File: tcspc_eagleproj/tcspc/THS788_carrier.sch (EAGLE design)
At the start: 46 parts, among them J1 BXE-040-01-F-D-A_BSE, U1 THS788

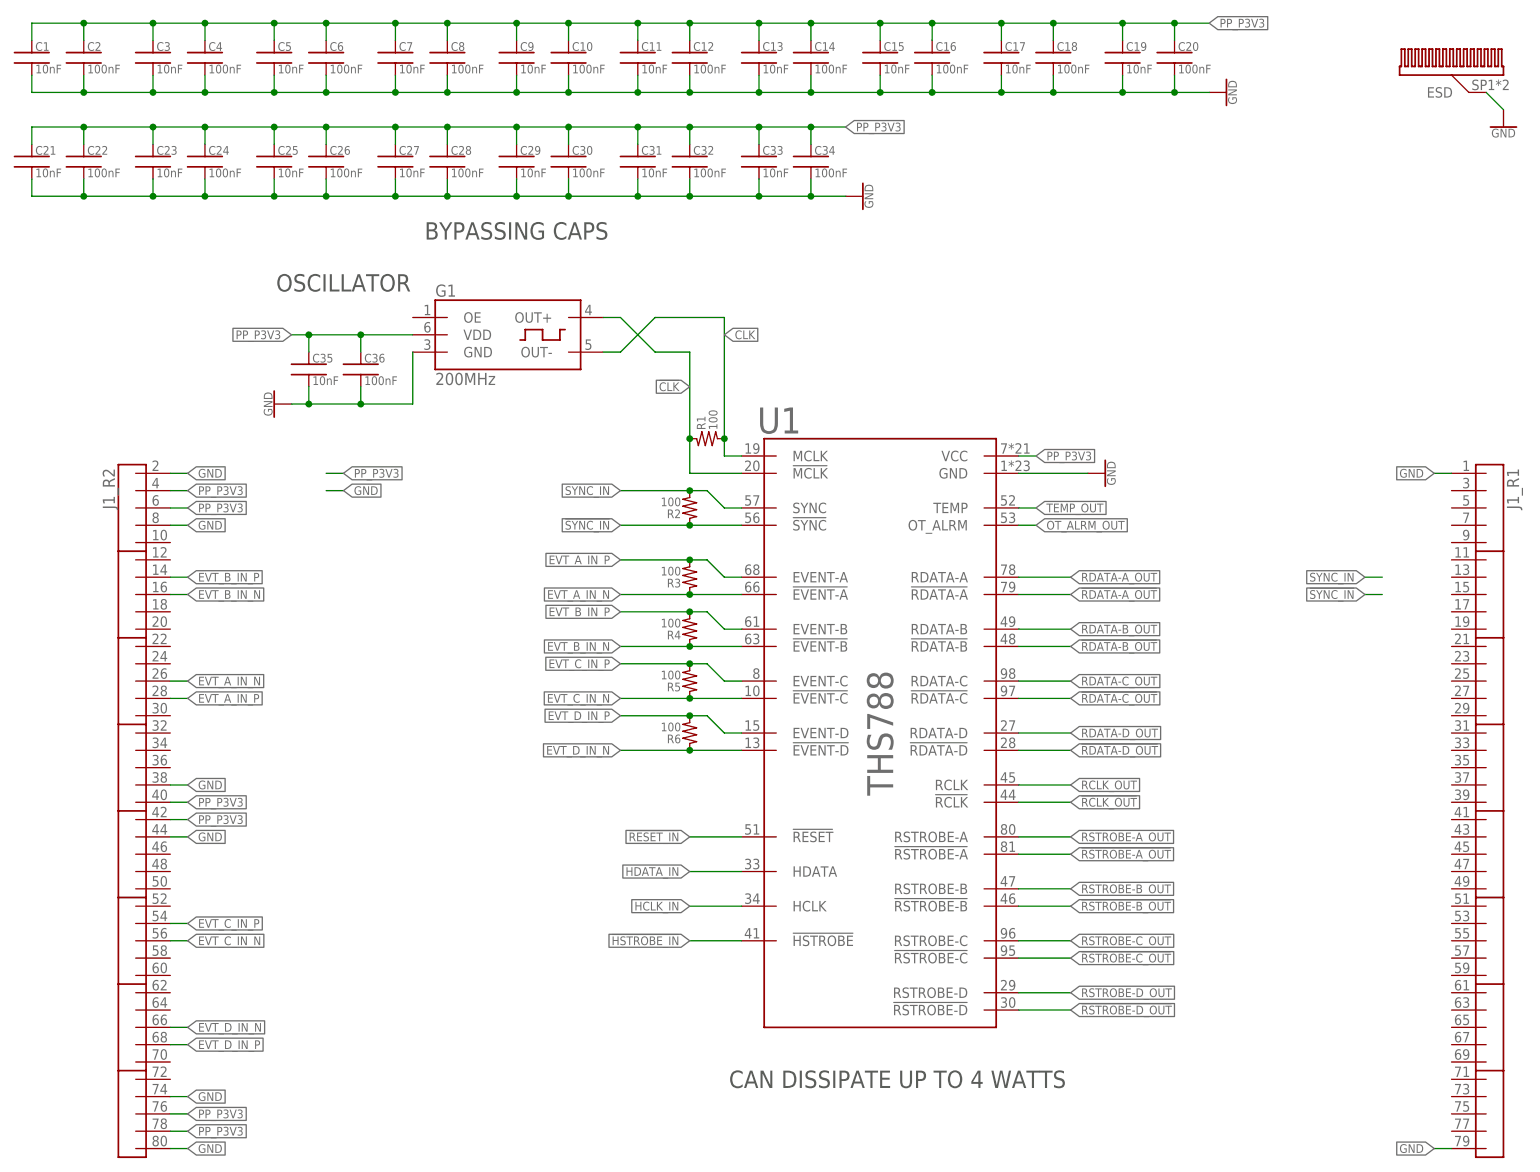
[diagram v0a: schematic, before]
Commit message: Did a little more work on the THS788 carrier, routed a few more HS diff signals
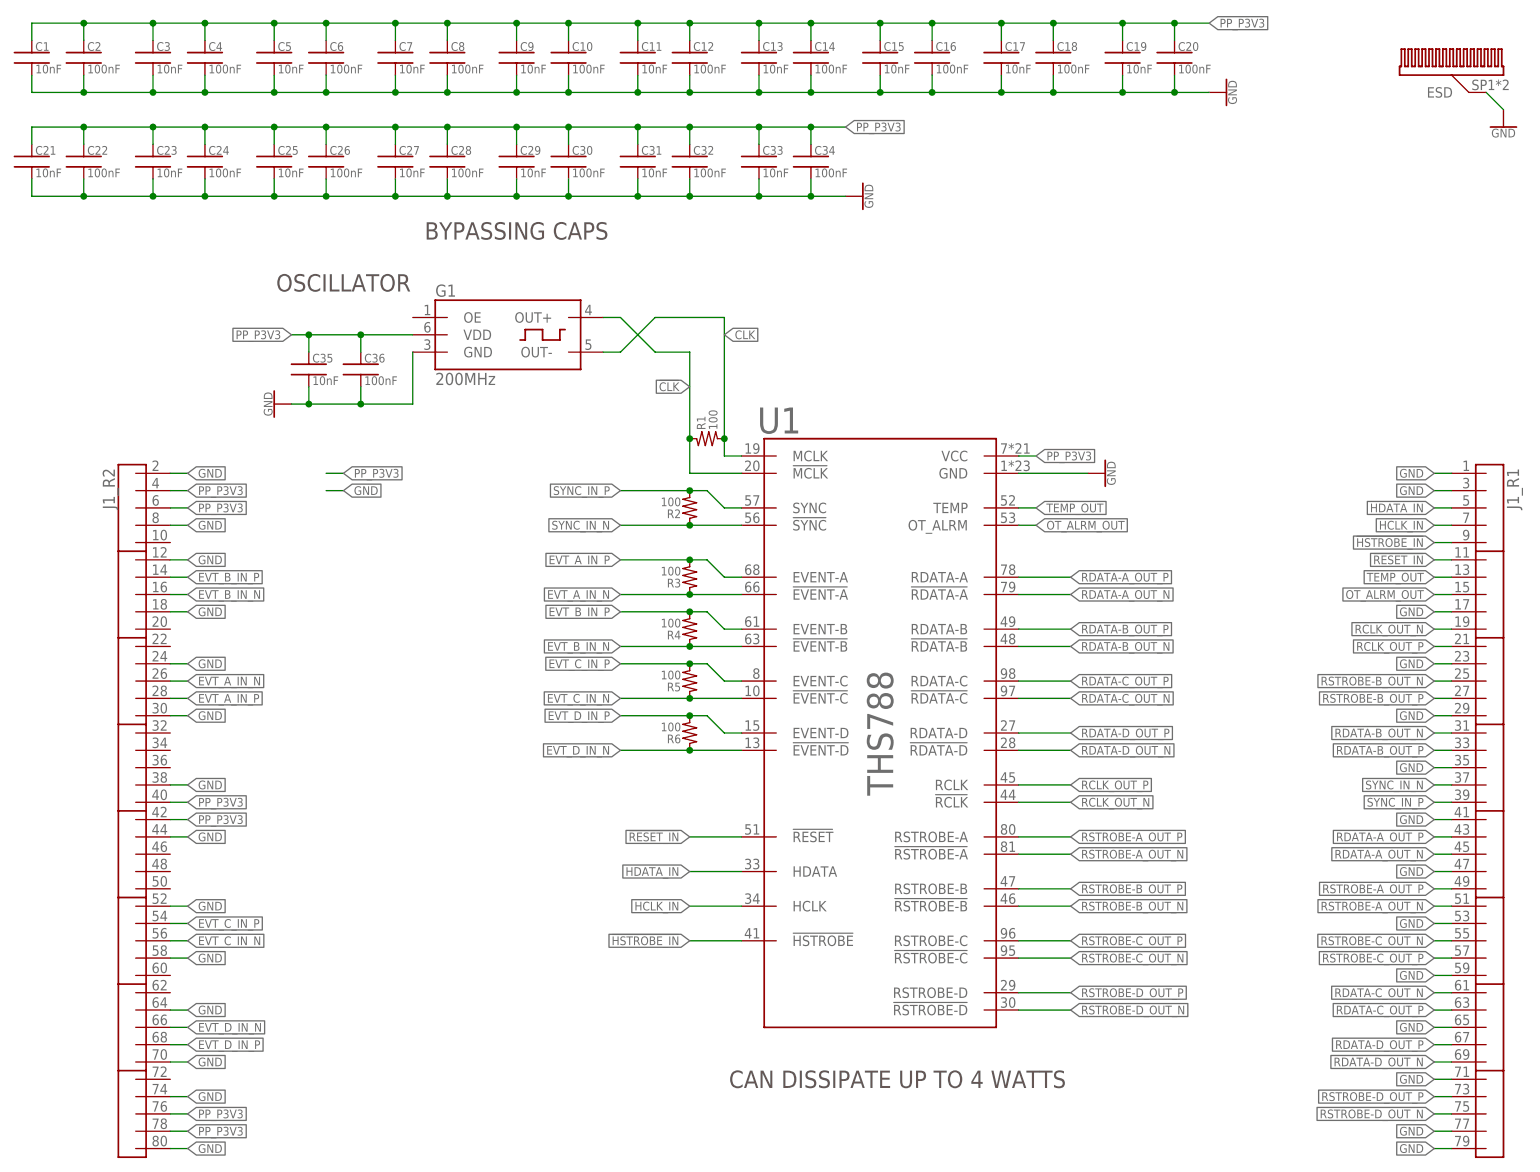
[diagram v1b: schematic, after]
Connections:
- removed net !RCLK_OUT: U1.!RCLK
- removed net !RDATA-A_OUT: U1.!RDATA-A
- removed net !RDATA-B_OUT: U1.!RDATA-B
- removed net !RDATA-C_OUT: U1.!RDATA-C
- removed net !RDATA-D_OUT: U1.!RDATA-D
- removed net !RSTROBE-A_OUT: U1.!RSTROBE-A
- removed net !RSTROBE-B_OUT: U1.!RSTROBE-B
- removed net !RSTROBE-C_OUT: U1.!RSTROBE-C
- removed net !RSTROBE-D_OUT: U1.!RSTROBE-D
- removed net !SYNC_IN: R2.1, U1.!SYNC
- removed net RCLK_OUT: U1.RCLK
- removed net RDATA-A_OUT: U1.RDATA-A
- removed net RDATA-B_OUT: U1.RDATA-B
- removed net RDATA-C_OUT: U1.RDATA-C
- removed net RDATA-D_OUT: U1.RDATA-D
- removed net RSTROBE-A_OUT: U1.RSTROBE-A
- removed net RSTROBE-B_OUT: U1.RSTROBE-B
- removed net RSTROBE-C_OUT: U1.RSTROBE-C
- removed net RSTROBE-D_OUT: U1.RSTROBE-D
- removed net SYNC_IN: R2.2, U1.SYNC
- new net RCLK_OUT_N: J1_R1.P10, U1.!RCLK
- new net RCLK_OUT_P: J1_R1.P11, U1.RCLK
- new net RDATA-A_OUT_N: J1_R1.P23, U1.!RDATA-A
- new net RDATA-A_OUT_P: J1_R1.P22, U1.RDATA-A
- new net RDATA-B_OUT_N: J1_R1.P16, U1.!RDATA-B
- new net RDATA-B_OUT_P: J1_R1.P17, U1.RDATA-B
- new net RDATA-C_OUT_N: J1_R1.P31, U1.!RDATA-C
- new net RDATA-C_OUT_P: J1_R1.P32, U1.RDATA-C
- new net RDATA-D_OUT_N: J1_R1.P35, U1.!RDATA-D
- new net RDATA-D_OUT_P: J1_R1.P34, U1.RDATA-D
- new net RSTROBE-A_OUT_N: J1_R1.P26, U1.!RSTROBE-A
- new net RSTROBE-A_OUT_P: J1_R1.P25, U1.RSTROBE-A
- new net RSTROBE-B_OUT_N: J1_R1.P13, U1.!RSTROBE-B
- new net RSTROBE-B_OUT_P: J1_R1.P14, U1.RSTROBE-B
- new net RSTROBE-C_OUT_N: J1_R1.P28, U1.!RSTROBE-C
- new net RSTROBE-C_OUT_P: J1_R1.P29, U1.RSTROBE-C
- new net RSTROBE-D_OUT_N: J1_R1.P38, U1.!RSTROBE-D
- new net RSTROBE-D_OUT_P: J1_R1.P37, U1.RSTROBE-D
- new net SYNC_IN_N: J1_R1.P19, R2.1, U1.!SYNC
- new net SYNC_IN_P: J1_R1.P20, R2.2, U1.SYNC
- net !HSTROBE_IN: now also J1_R1.P5
- net !RESET_IN: now also J1_R1.P6
- net GND: now also J1_R1.P12, J1_R1.P15, J1_R1.P18, J1_R1.P2, J1_R1.P21, J1_R1.P24, J1_R1.P27, J1_R1.P30, J1_R1.P33, J1_R1.P36, J1_R1.P39, J1_R1.P9, J1_R2.P12, J1_R2.P15, J1_R2.P26, J1_R2.P29, J1_R2.P32, J1_R2.P35, J1_R2.P6, J1_R2.P9
- net HCLK_IN: now also J1_R1.P4
- net HDATA_IN: now also J1_R1.P3
- net OT_ALRM_OUT: now also J1_R1.P8
- net TEMP_OUT: now also J1_R1.P7
